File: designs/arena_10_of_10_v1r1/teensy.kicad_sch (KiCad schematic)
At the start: 41 parts, among them J1 Cetus RJ45 Magjack, J2 Conn_01x02, J3 Conn_Coaxial, J30 Conn_01x02, J4 Conn_Coaxial, U1 Teensy4.1, U2 SN74LVC1T45DBV, U3 SN74LVC1T45DBV

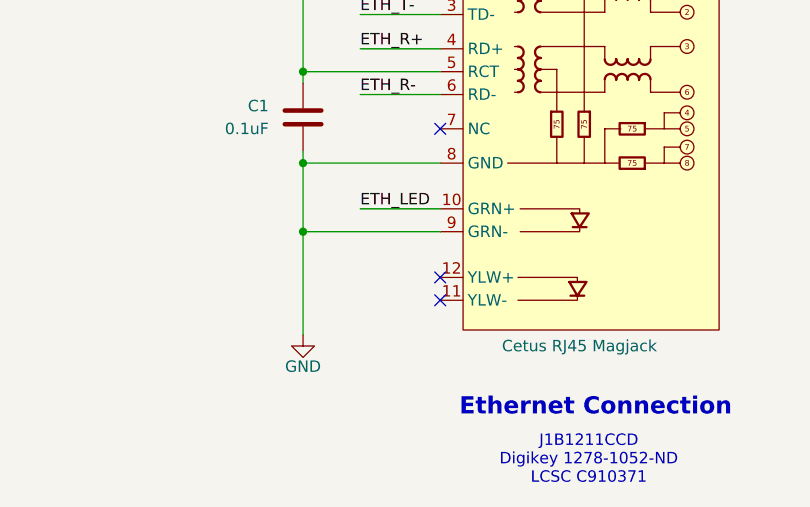
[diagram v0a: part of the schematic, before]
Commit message: Tightened DRC rules, increased via sizes, and added switch
Added power switch SW1.

Assemble pin sockets for Teensy (J100/J101, 1x24 pin sockets; J102, 2x3 pin socket, 2mm pitch for ethernet).

Tightened board-setup DRC limits to match JLCPCB 6-layer minimums:

- min_hole_to_hole 0.25 -> 0.5 mm,
- min_text_thickness 0.08 -> 0.15 mm,
- min_via_annular_width 0.05 -> 0.075 mm.

Set stackup copper_finish from "None" to "ENIG".

Added PCB title block and automatic name / revision / date on silkscreen.

Refreshed footprints from library (0402/1210/SOT-23 crtyd now  uses fp_rect).

produced v1.1.2.
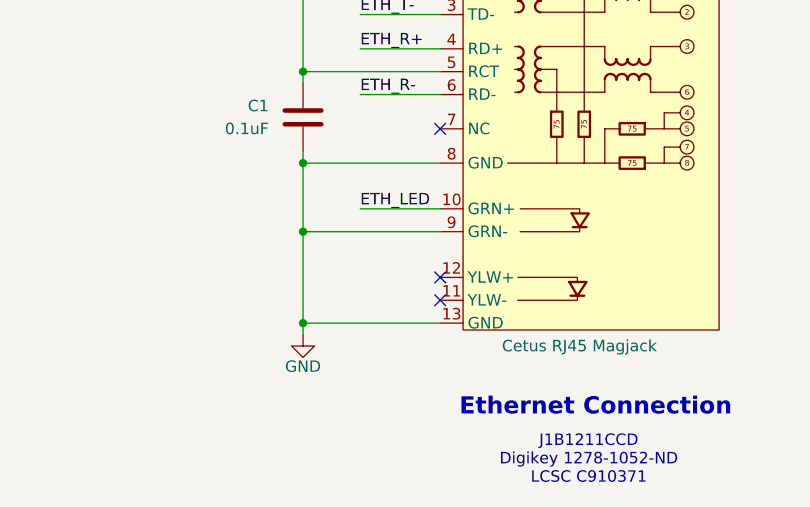
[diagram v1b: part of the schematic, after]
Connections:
- net GND: now also J1.13 (GND)
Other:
- company: (none) -> IORodeo for Reiser Lab @ Janelia | HHMI
- title: (none) -> G6 Teensy 10-10 Arena
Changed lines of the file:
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@@
 	(generator_version "9.0")
 	(paper "USLetter")
+	(title_block
+		(title "G6 Teensy 10-10 Arena")
+		(date "2026-04-22")
+		(rev "v1.1.2")
+		(company "IORodeo for Reiser Lab @ Janelia | HHMI")
+	)
 	(bus_alias "I2C"
 		(members "SCL" "SDA")
@@
 	)
 	(junction
+		(at 54.61 179.07)
+		(diameter 0)
+		(color 0 0 0 0)
+	)
+	(junction
 		(at 144.78 135.89)
 		(diameter 0)
@@
 	(wire
 		(pts
-			(xy 54.61 168.91) (xy 54.61 180.34)
+			(xy 54.61 168.91) (xy 54.61 179.07)
 		)
 		(stroke
@@
 	(wire
 		(pts
+			(xy 54.61 179.07) (xy 54.61 180.34)
+		)
+		(stroke
+			(width 0)
+			(type default)
+		)
+	)
+	(wire
+		(pts
 			(xy 30.48 53.34) (xy 43.18 53.34)
 		)
@@
 	(wire
 		(pts
+			(xy 54.61 179.07) (xy 69.85 179.07)
+		)
+		(stroke
+			(width 0)
+			(type default)
+		)
+	)
+	(wire
+		(pts
 			(xy 30.48 45.72) (xy 43.18 45.72)
 		)
@@
 		)
 		(instances
-			(project ""
+			(project "arena_10_of_10_v1r1"
 				(path "/056666d2-2c8f-491c-bcad-db3c517779a8/49d7122d-250d-4ac4-9432-46d5d4ec4ae4"
 					(reference "#PWR013")
@@
 		)
 		(instances
-			(project ""
+			(project "arena_10_of_10_v1r1"
 				(path "/056666d2-2c8f-491c-bcad-db3c517779a8/49d7122d-250d-4ac4-9432-46d5d4ec4ae4"
 					(reference "J2")
@@
 		(pin "7"
 		)
+		(pin "13"
+		)
 		(instances
-			(project ""
+			(project "arena_10_of_10_v1r1"
 				(path "/056666d2-2c8f-491c-bcad-db3c517779a8/49d7122d-250d-4ac4-9432-46d5d4ec4ae4"
 					(reference "J1")
@@
 		)
 		(instances
-			(project ""
+			(project "arena_10_of_10_v1r1"
 				(path "/056666d2-2c8f-491c-bcad-db3c517779a8/49d7122d-250d-4ac4-9432-46d5d4ec4ae4"
 					(reference "J3")
@@
 		)
 		(instances
-			(project ""
+			(project "arena_10_of_10_v1r1"
 				(path "/056666d2-2c8f-491c-bcad-db3c517779a8/49d7122d-250d-4ac4-9432-46d5d4ec4ae4"
 					(reference "#PWR01")
@@
 		)
 		(instances
-			(project ""
+			(project "arena_10_of_10_v1r1"
 				(path "/056666d2-2c8f-491c-bcad-db3c517779a8/49d7122d-250d-4ac4-9432-46d5d4ec4ae4"
 					(reference "U1")
@@
 		)
 		(instances
-			(project ""
+			(project "arena_10_of_10_v1r1"
 				(path "/056666d2-2c8f-491c-bcad-db3c517779a8/49d7122d-250d-4ac4-9432-46d5d4ec4ae4"
 					(reference "U2")
@@
 		)
 		(instances
-			(project ""
+			(project "arena_10_of_10_v1r1"
 				(path "/056666d2-2c8f-491c-bcad-db3c517779a8/49d7122d-250d-4ac4-9432-46d5d4ec4ae4"
 					(reference "R1")
